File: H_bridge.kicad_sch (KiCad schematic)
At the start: 23 parts, among them J1 Conn_01x04_Socket, J2 Conn_01x04_Socket, J3 Conn_01x04_Socket, J4 Conn_01x04_Socket, J5 Conn_01x04_Socket, J6 Conn_01x04_Socket, J7 Conn_01x04_Socket, U1 VNH7040AYTR

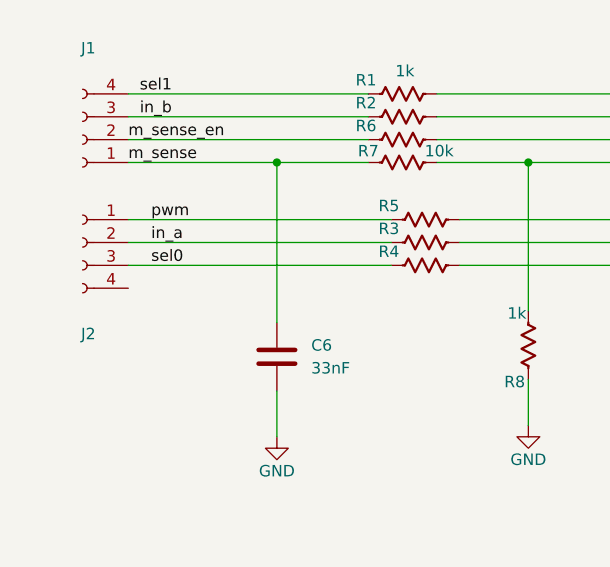
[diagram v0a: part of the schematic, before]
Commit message: Primera version preliminar Conexiones y cobre completado Falta verificar las reglas y el BOM
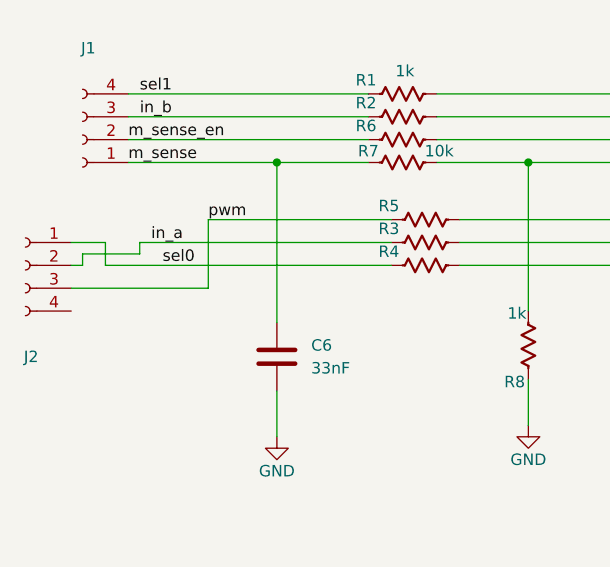
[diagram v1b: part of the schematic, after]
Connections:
- net pwm: now also J2.3 (Pin_3); no longer J2.1 (Pin_1)
- net sel0: now also J2.1 (Pin_1); no longer J2.3 (Pin_3)
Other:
- company: (none) -> ITLA-HUB
- title: (none) -> VNH7040_Puente_H_RC
- moved on the sheet: J2
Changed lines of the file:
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@@
 	(generator "eeschema")
 	(generator_version "9.0")
-	(paper "A4")
+	(paper "A")
+	(title_block
+		(title "VNH7040_Puente_H_RC")
+		(date "2025-11-16")
+		(rev "1.0")
+		(company "ITLA-HUB")
+	)
 	(text "Puente H\n"
 		(exclude_from_sim no)
@@
 	(wire
 		(pts
+			(xy 60.96 87.63) (xy 88.9 87.63)
+		)
+		(stroke
+			(width 0)
+			(type default)
+		)
+	)
+	(wire
+		(pts
 			(xy 189.23 120.65) (xy 185.42 120.65)
 		)
@@
 	(wire
 		(pts
+			(xy 68.58 85.09) (xy 88.9 85.09)
+		)
+		(stroke
+			(width 0)
+			(type default)
+		)
+	)
+	(wire
+		(pts
 			(xy 177.8 101.6) (xy 177.8 99.06)
 		)
@@
 	(wire
 		(pts
-			(xy 59.69 87.63) (xy 88.9 87.63)
-		)
-		(stroke
-			(width 0)
-			(type default)
-		)
-	)
-	(wire
-		(pts
 			(xy 124.46 125.73) (xy 116.84 125.73)
 		)
@@
 	(wire
 		(pts
+			(xy 57.15 87.63) (xy 53.34 87.63)
+		)
+		(stroke
+			(width 0)
+			(type default)
+		)
+	)
+	(wire
+		(pts
 			(xy 177.8 86.36) (xy 181.61 86.36)
 		)
@@
 	(wire
 		(pts
+			(xy 54.61 90.17) (xy 54.61 88.9)
+		)
+		(stroke
+			(width 0)
+			(type default)
+		)
+	)
+	(wire
+		(pts
 			(xy 104.14 78.74) (xy 104.14 95.25)
 		)
@@
 	(wire
 		(pts
+			(xy 53.34 92.71) (xy 68.58 92.71)
+		)
+		(stroke
+			(width 0)
+			(type default)
+		)
+	)
+	(wire
+		(pts
 			(xy 177.8 76.2) (xy 177.8 73.66)
 		)
@@
 	(wire
 		(pts
-			(xy 59.69 90.17) (xy 88.9 90.17)
-		)
-		(stroke
-			(width 0)
-			(type default)
-		)
-	)
-	(wire
-		(pts
 			(xy 104.14 125.73) (xy 104.14 129.54)
 		)
@@
 	(wire
 		(pts
+			(xy 57.15 90.17) (xy 57.15 87.63)
+		)
+		(stroke
+			(width 0)
+			(type default)
+		)
+	)
+	(wire
+		(pts
 			(xy 116.84 54.61) (xy 116.84 57.15)
 		)
@@
 	(wire
 		(pts
+			(xy 60.96 88.9) (xy 60.96 87.63)
+		)
+		(stroke
+			(width 0)
+			(type default)
+		)
+	)
+	(wire
+		(pts
 			(xy 176.53 68.58) (xy 176.53 66.04)
 		)
@@
 	(wire
 		(pts
+			(xy 57.15 90.17) (xy 88.9 90.17)
+		)
+		(stroke
+			(width 0)
+			(type default)
+		)
+	)
+	(wire
+		(pts
 			(xy 185.42 128.27) (xy 185.42 133.35)
 		)
@@
 	(wire
 		(pts
-			(xy 59.69 85.09) (xy 88.9 85.09)
-		)
-		(stroke
-			(width 0)
-			(type default)
-		)
-	)
-	(wire
-		(pts
 			(xy 104.14 78.74) (xy 133.35 78.74)
 		)
@@
 	(wire
 		(pts
+			(xy 53.34 90.17) (xy 54.61 90.17)
+		)
+		(stroke
+			(width 0)
+			(type default)
+		)
+	)
+	(wire
+		(pts
 			(xy 160.02 121.92) (xy 162.56 121.92)
 		)
@@
 	(wire
 		(pts
+			(xy 54.61 88.9) (xy 60.96 88.9)
+		)
+		(stroke
+			(width 0)
+			(type default)
+		)
+	)
+	(wire
+		(pts
 			(xy 207.01 68.58) (xy 204.47 68.58)
 		)
@@
 		)
 	)
+	(wire
+		(pts
+			(xy 68.58 92.71) (xy 68.58 85.09)
+		)
+		(stroke
+			(width 0)
+			(type default)
+		)
+	)
 	(label "sel0"
-		(at 62.23 90.17 0)
+		(at 63.5 90.17 0)
 		(effects
 			(font
@@
 	)
 	(label "pwm"
-		(at 62.23 85.09 0)
+		(at 68.58 85.09 0)
 		(effects
 			(font
@@
 	(symbol
 		(lib_id "Connector:Conn_01x04_Socket")
-		(at 54.61 87.63 0)
+		(at 48.26 90.17 0)
 		(mirror y)
 		(unit 1)
@@
 		(dnp no)
 		(property "Reference" "J2"
-			(at 55.245 97.79 0)
+			(at 48.895 100.33 0)
 			(effects
 				(font
@@
 		)
 		(property "Value" "Conn_01x04_Socket"
-			(at 55.245 95.25 0)
+			(at 48.895 97.79 0)
 			(effects
 				(font
@@
 		)
 		(property "Footprint" "Connector_PinSocket_1.27mm:PinSocket_1x04_P1.27mm_Castellated"
-			(at 54.61 87.63 0)
+			(at 48.26 90.17 0)
 			(effects
 				(font
@@
 		)
 		(property "Datasheet" "~"
-			(at 54.61 87.63 0)
+			(at 48.26 90.17 0)
 			(effects
 				(font
@@
 		)
 		(property "Description" "Generic connector, single row, 01x04, script generated"
-			(at 54.61 87.63 0)
+			(at 48.26 90.17 0)
 			(effects
 				(font
@@
 		)
 		(property "VOL" ""
-			(at 54.61 87.63 0)
+			(at 48.26 90.17 0)
 			(effects
 				(font
@@
 		)
 		(property "TOL" ""
-			(at 54.61 87.63 0)
+			(at 48.26 90.17 0)
 			(effects
 				(font
@@
 		)
 		(property "CURRENT" ""
-			(at 54.61 87.63 0)
+			(at 48.26 90.17 0)
 			(effects
 				(font
@@
 		)
 		(property "Part Number" ""
-			(at 54.61 87.63 0)
+			(at 48.26 90.17 0)
 			(effects
 				(font
@@
 		)
 		(property "Verificado" ""
-			(at 54.61 87.63 0)
+			(at 48.26 90.17 0)
 			(effects
 				(font
@@
 		)
 		(property "Manufacturer" ""
-			(at 54.61 87.63 0)
+			(at 48.26 90.17 0)
 			(effects
 				(font
@@
 		)
 		(property "LCSC PN" ""
-			(at 54.61 87.63 0)
-			(effects
-				(font
+			(at 48.26 90.17 0)
+			(effects
+				(font

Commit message: Actualizaciones de diseno genetrales.
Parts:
- added J8: Conn_01x04_Socket, Connector_PinSocket_1.27mm:PinSocket_1x04_P1.27mm_Castellated, symbol Connector:Conn_01x04_Socket
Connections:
- net GND: now also J2.4 (Pin_4), J8.1 (Pin_1), J8.2 (Pin_2), J8.3 (Pin_3), J8.4 (Pin_4)
- net pwm: now also J2.1 (Pin_1); no longer J2.3 (Pin_3)
- net sel0: now also J2.3 (Pin_3); no longer J2.1 (Pin_1)
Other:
- moved on the sheet: J2, J4, J7

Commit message: Completado el BOM
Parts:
- C1, C2, C4, C5: value C_0805 -> 100NF; LCSC Part (none) -> C1853551; VOL (none) -> 100V
- C3: LCSC Part (none) -> C22469994
- C6: LCSC Part (none) -> C576851; VOL (none) -> 50V
- D2: LCSC Part (none) -> C151259
- J1, J2, J3, J4, J5, J6, J7, J8: now left out of the parts list
- R1, R8: value 1k -> 1K; LCSC Part (none) -> C22548
- R2, R3, R4, R5, R6: value R_0603 -> 1K; LCSC Part (none) -> C22548
- R7: value 10k -> 10K; LCSC Part (none) -> C98220
- U1: LCSC Part (none) -> C2969764

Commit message: Version 1 enviada a fabricacion
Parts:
- removed C1, C2: 100NF, Capacitor_SMD_AKL:C_0805_2012Metric, symbol Capacitor_AKL:C_0805
- R8: value 1K -> 1.5K; LCSC Part C22548 -> C114668
